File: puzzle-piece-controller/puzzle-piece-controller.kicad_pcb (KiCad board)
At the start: 2 copper layers, 10 parts, among them J1 POGO PINS, J2 OUTPUT_1, J4 BUTTON, J5 Conn_01x04_Socket, U1 MOUDLE-SEEEDUINO-XIAO-ESP32C3

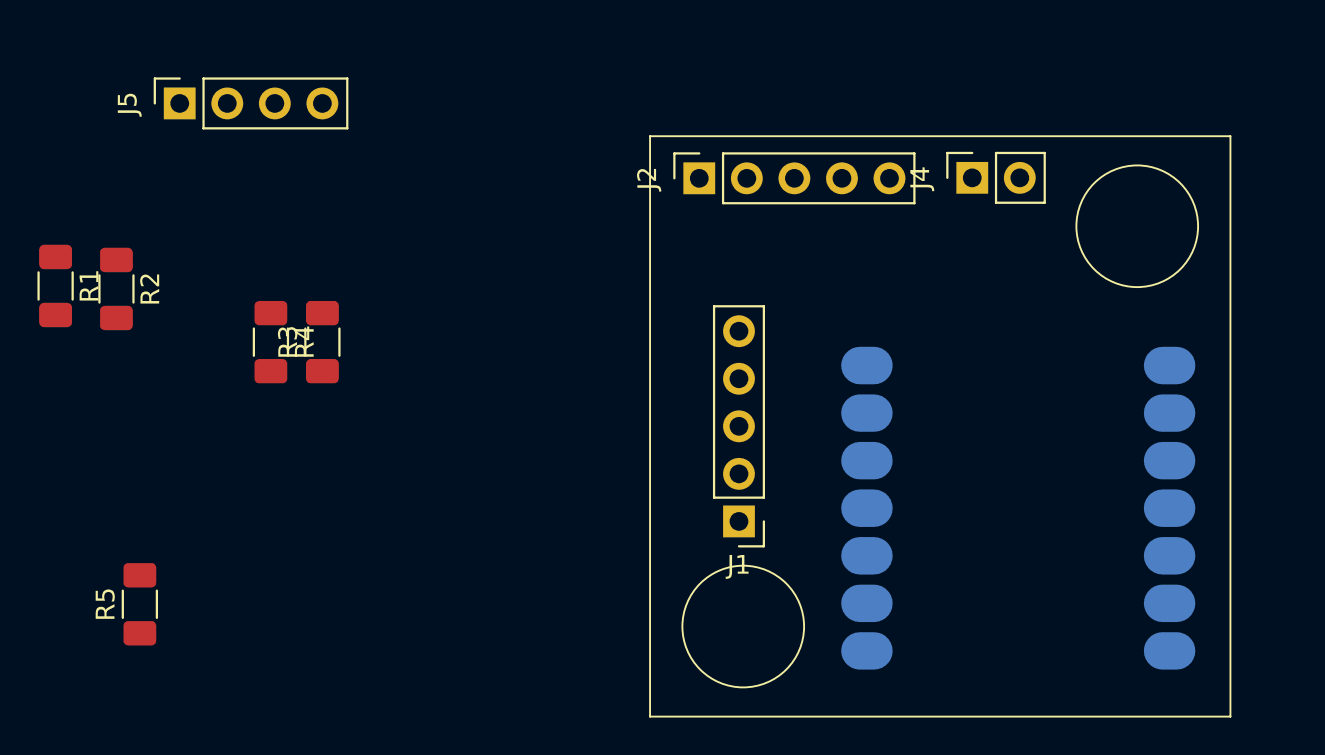
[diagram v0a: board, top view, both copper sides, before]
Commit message: made battery controller singled sided and removed lipo
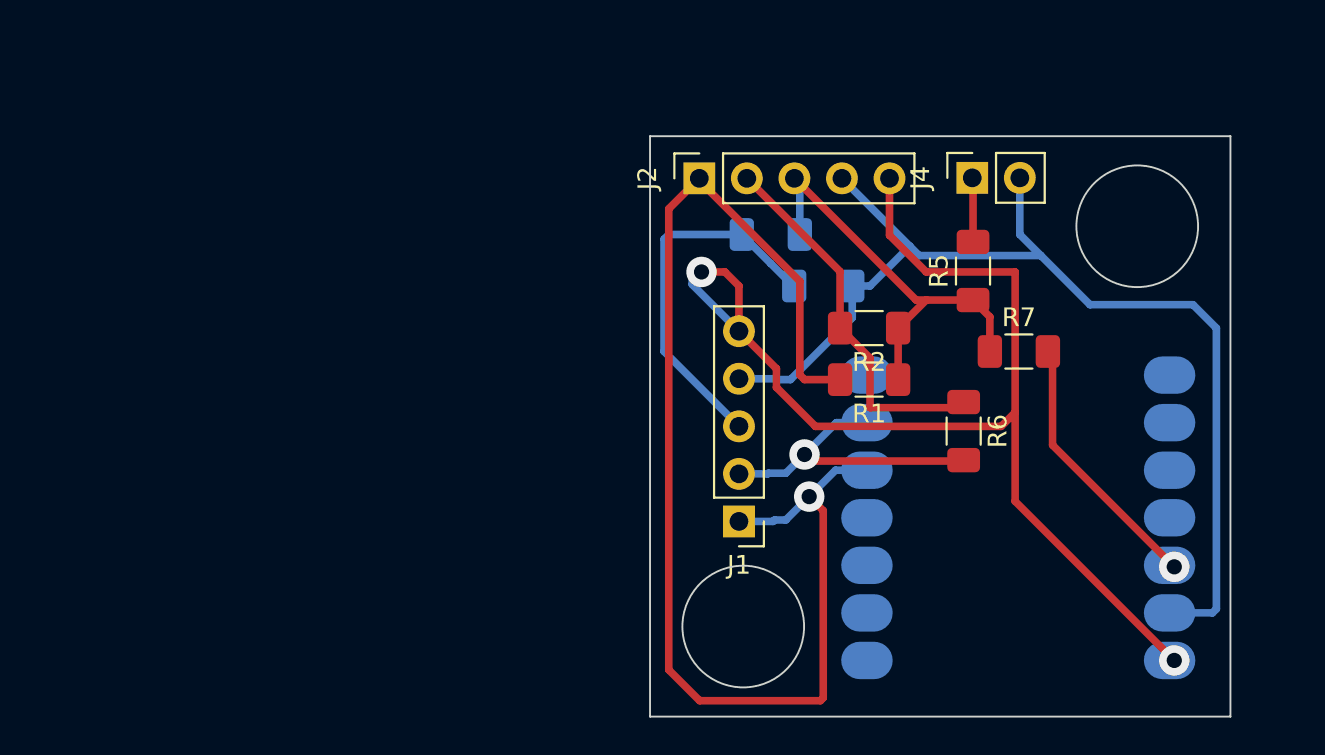
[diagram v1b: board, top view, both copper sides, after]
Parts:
- removed J5: Conn_01x04_Socket, Connector_PinSocket_2.54mm:PinSocket_1x04_P2.54mm_Vertical
- added R6: 0, Resistor_SMD:R_1206_3216Metric_Pad1.30x1.75mm_HandSolder, F.Cu at (224.2, 90.8)
- added R7: 0, Resistor_SMD:R_1206_3216Metric_Pad1.30x1.75mm_HandSolder, F.Cu at (227.2, 86.5)
- R3, R4: moved to B.Cu
- moved R5 47.9 mm to (224.8, 82.2)
- moved R1 43.7 mm to (219.2, 88.0), turned to 180 degrees
- moved R2 40.3 mm to (219.2, 85.2), turned to 180 degrees
- moved R4 29.7 mm to (216.8, 83.0), turned to 0 degrees
- moved R3 24.6 mm to (213.9, 80.2), turned to 180 degrees
- moved U1 0.51 mm to (218.2, 84.9)
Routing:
- net H_SDA: track 0.00 -> 69.9 mm, vias 0 -> 1
- net +5V: track 0.00 -> 62.5 mm, vias 0 -> 2
- net GND: track 0.00 -> 58.6 mm
- net +3.3V: track 0.00 -> 36.8 mm, vias 0 -> 1
- net H_SCL: track 0.00 -> 35.7 mm, vias 0 -> 1
- net ANALOG: track 0.00 -> 19.8 mm
- net Net-(J4-Pin_1): track 0.00 -> 3.44 mm
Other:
- board outline added: 31 x 31 mm

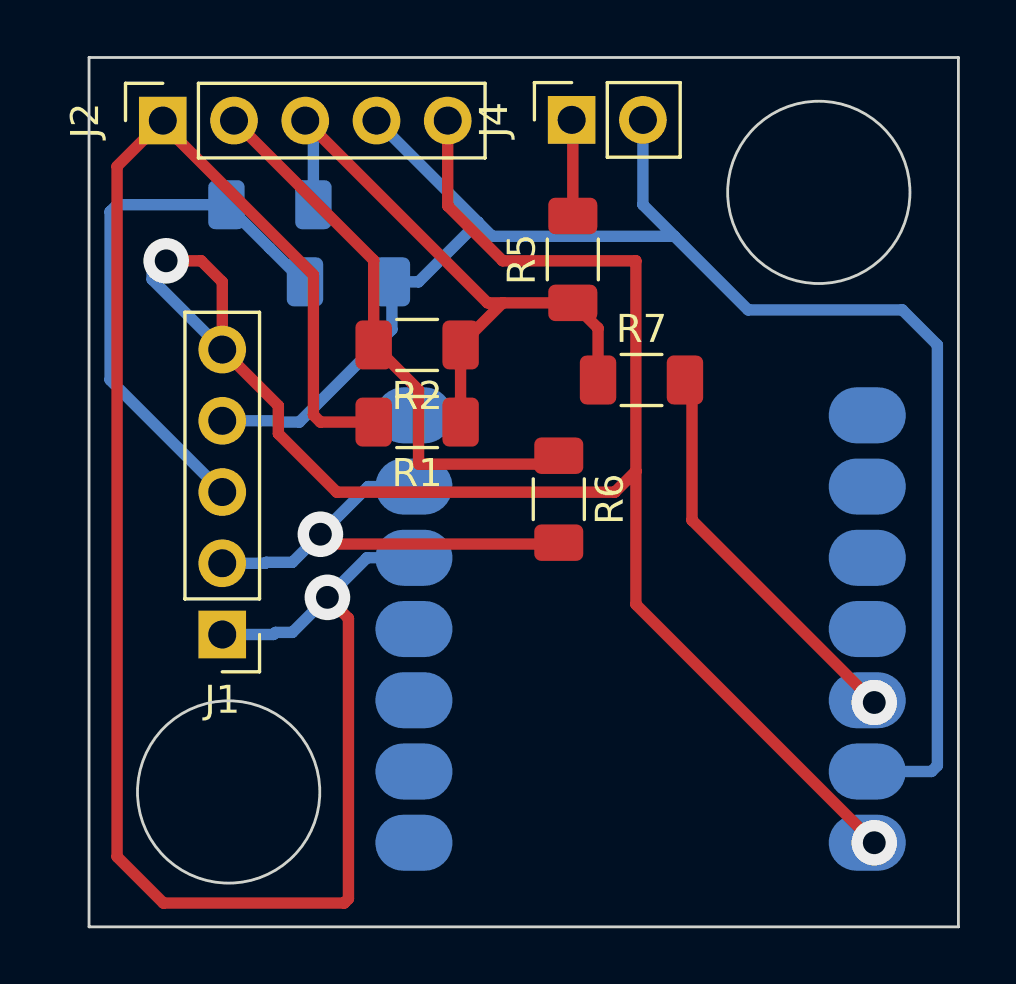
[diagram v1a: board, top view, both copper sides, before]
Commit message: made controller pcb single sided
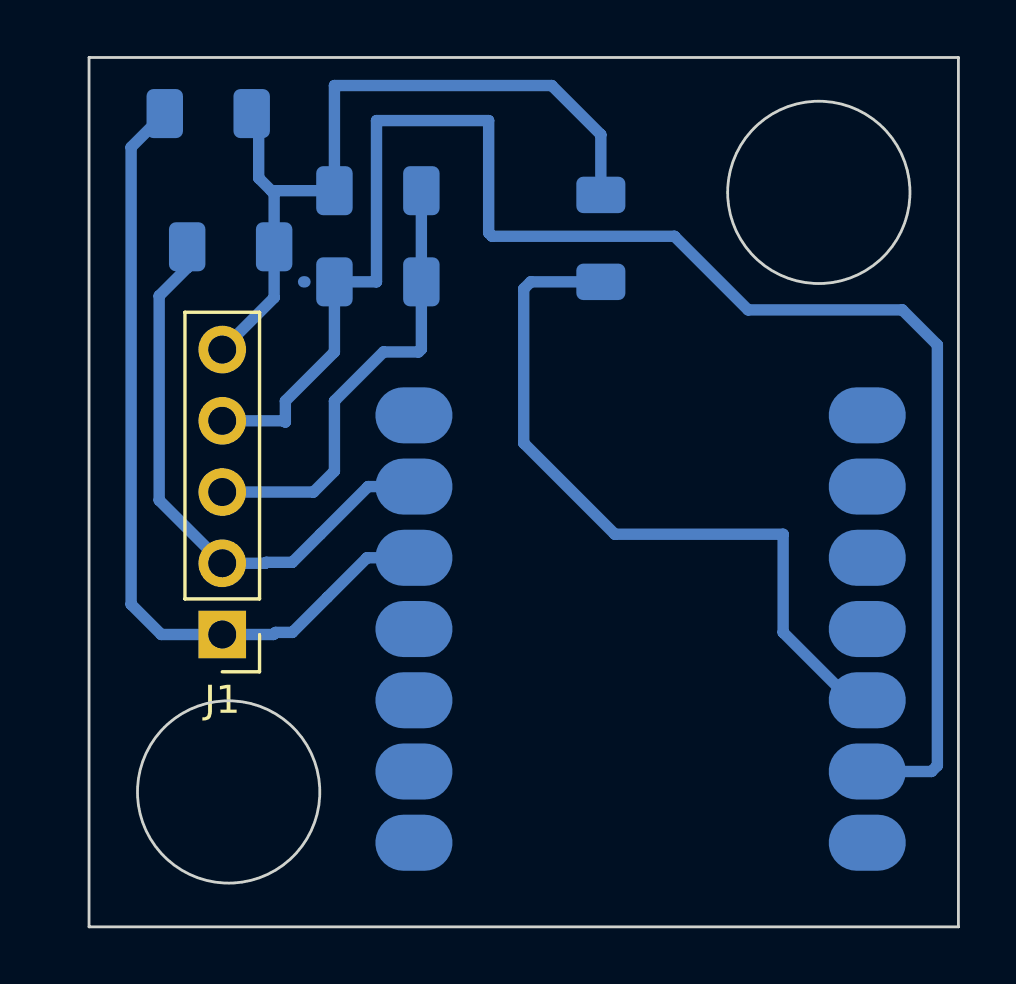
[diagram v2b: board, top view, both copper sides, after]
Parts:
- removed J2: OUTPUT_1, Connector_PinSocket_2.54mm:PinSocket_1x05_P2.54mm_Vertical
- removed J4: BUTTON, Connector_PinSocket_2.54mm:PinSocket_1x02_P2.54mm_Vertical
- removed R5: 10K, Resistor_SMD:R_1206_3216Metric_Pad1.30x1.75mm_HandSolder
- removed R6: 0, Resistor_SMD:R_1206_3216Metric_Pad1.30x1.75mm_HandSolder
- R1, R2, R7: moved to B.Cu
- moved R1 13.3 mm to (211.8, 77.0)
- moved R2 7.51 mm to (212.6, 81.8)
- moved R7 5.25 mm to (225.8, 81.5), turned to -90 degrees
- moved R3 3.88 mm to (217.8, 79.8), turned to 0 degrees
- moved R4 1.05 mm to (217.8, 83.0), turned to 180 degrees
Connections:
- J1 pad 5: +5V -> +3.3V
- U1 pad 1: Net-(J4-Pin_1) -> unconnected-(U1-PA02_A0_D0-Pad1)
- U1 pad 14: +5V -> unconnected-(U1-5V-Pad14)
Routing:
- net +5V: track 62.5 -> 0.00 mm, vias 2 -> 0
- net H_SDA: track 69.9 -> 29.7 mm, vias 1 -> 0
- net +3.3V: track 36.8 -> 54.2 mm, vias 1 -> 0
- net H_SCL: track 35.7 -> 20.6 mm, vias 1 -> 0
- net ANALOG: track 19.8 -> 16.4 mm
- net Net-(J4-Pin_1): track 3.44 -> 0.00 mm

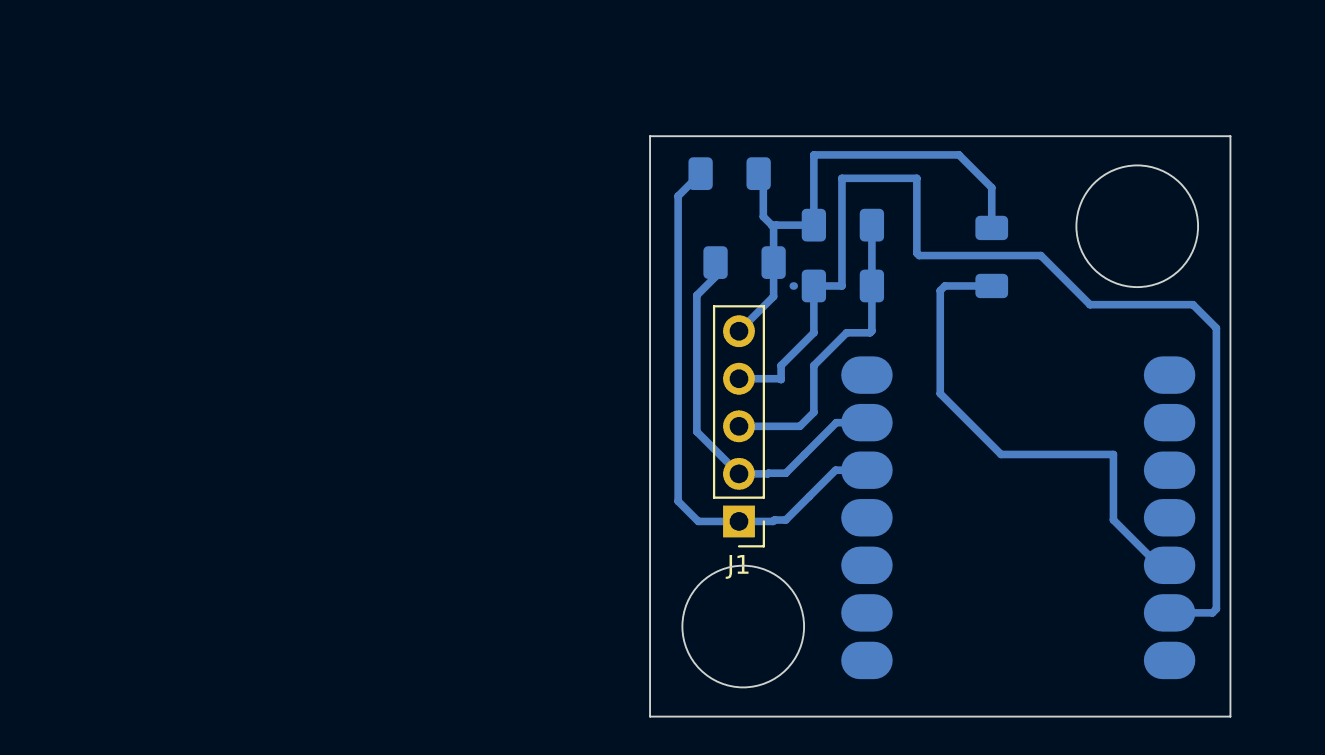
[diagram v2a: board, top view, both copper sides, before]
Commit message: add unrouted output throughholes to controller, and mounting holes
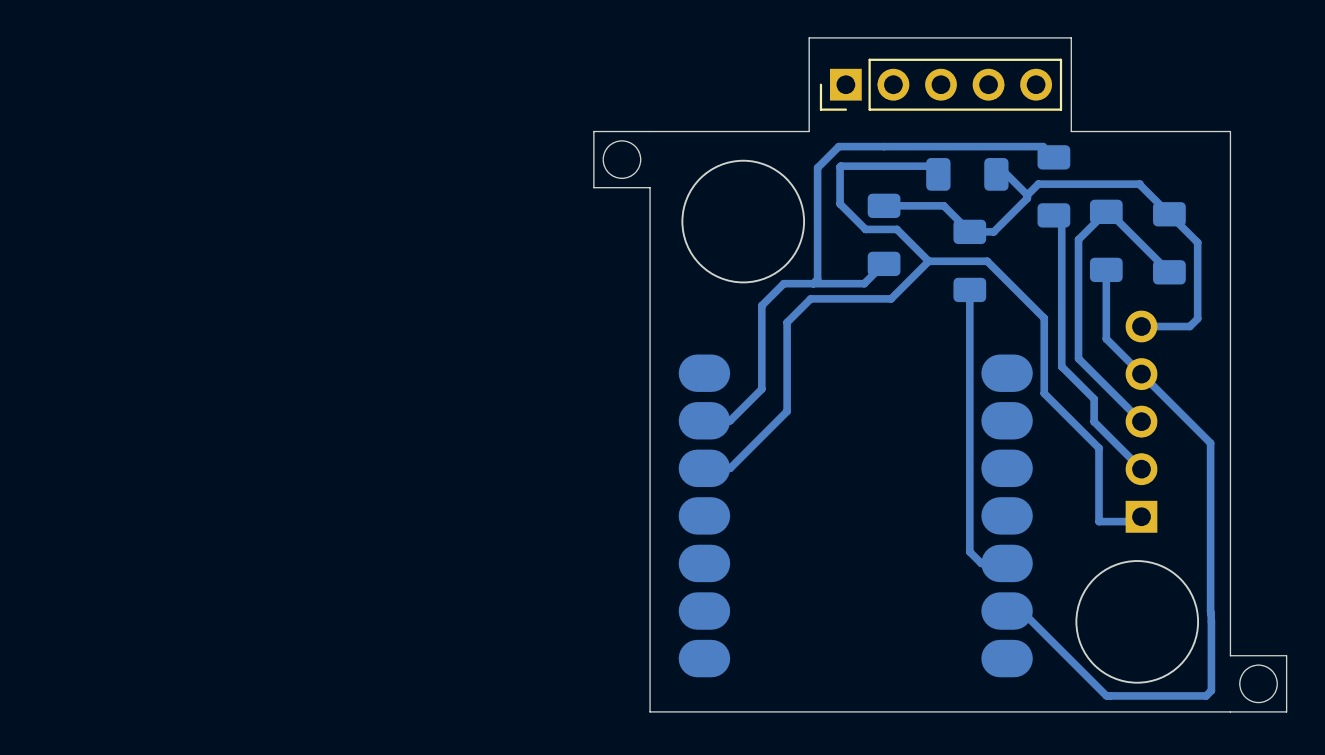
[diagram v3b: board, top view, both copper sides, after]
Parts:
- added J2: OUTPUT, Connector_PinHeader_2.54mm:PinHeader_1x05_P2.54mm_Vertical, F.Cu at (218.0, 72.2)
- added R5: 0, Resistor_SMD:R_1206_3216Metric_Pad1.30x1.75mm_HandSolder, B.Cu at (229.1, 77.7)
- J1: moved to B.Cu
- moved J1 21.5 mm to (233.8, 95.3), turned to 0 degrees
- moved R3 17.5 mm to (235.2, 80.7), turned to -90 degrees
- moved R4 14.3 mm to (231.9, 80.6), turned to -90 degrees
- moved R1 12.7 mm to (224.4, 77.0)
- moved U1 8.68 mm to (209.6, 84.8)
- moved R2 7.60 mm to (220.0, 80.3), turned to -90 degrees
- moved R7 1.19 mm to (224.6, 81.7)
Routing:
- net H_SCL: track 20.6 -> 50.8 mm
- net H_SDA: track 29.7 -> 54.7 mm
- net GND: track 58.5 -> 37.7 mm
- net +3.3V: track 54.2 -> 45.4 mm
- net ANALOG: track 16.4 -> 17.9 mm
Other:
- board size 31 x 31 mm -> 37 x 36 mm

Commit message: made puzzle-controller board double sided
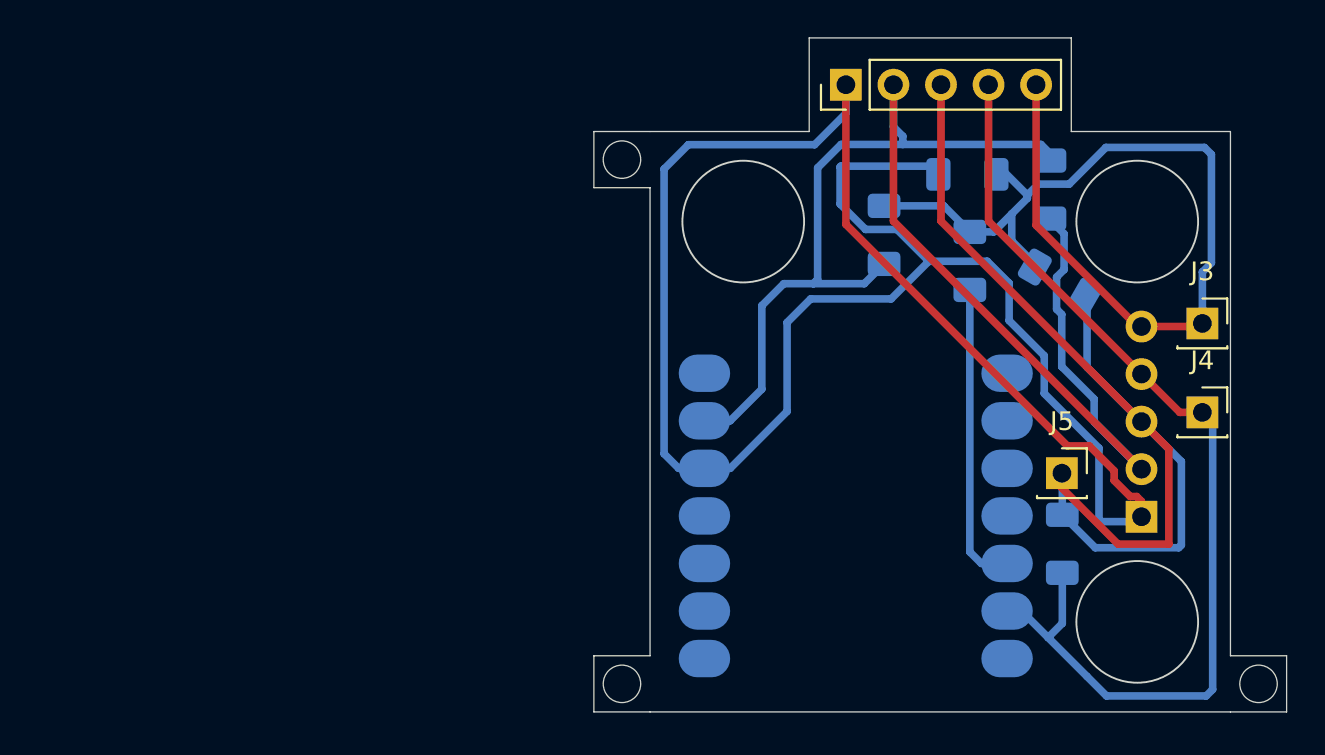
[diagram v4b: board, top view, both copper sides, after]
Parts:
- added J3: 3.3V, Connector_PinSocket_2.54mm:PinSocket_1x01_P2.54mm_Vertical, F.Cu at (237.0, 85.0)
- added J4: GND, Connector_PinSocket_2.54mm:PinSocket_1x01_P2.54mm_Vertical, F.Cu at (237.0, 89.8)
- added J5: ANALOG, Connector_PinSocket_2.54mm:PinSocket_1x01_P2.54mm_Vertical, F.Cu at (229.5, 93.0)
- moved R4 16.3 mm to (229.5, 96.8)
- moved R3 6.19 mm to (229.4, 82.8), turned to -30 degrees
- moved R5 0.27 mm to (228.9, 77.8)
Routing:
- net H_SDA: track 54.7 -> 115.3 mm
- net ANALOG: track 17.9 -> 62.1 mm
- net H_SCL: track 50.8 -> 80.8 mm
- net +3.3V: track 45.4 -> 70.1 mm
- net GND: track 37.7 -> 54.7 mm
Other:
- outline, holes or cut-outs redrawn

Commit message: current puzzle with attiny and pogo pins
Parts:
- removed J5: ANALOG, Connector_PinSocket_2.54mm:PinSocket_1x01_P2.54mm_Vertical
- added J6: OUTPUT, Connector_PinSocket_2.54mm:PinSocket_1x04_P2.54mm_Vertical, F.Cu at (219.1, 71.8)
- J1: moved to F.Cu
- J2: value OUTPUT -> ANALOG; footprint Connector_PinHeader_2.54mm:PinHeader_1x05_P2.54mm_Vertical -> Connector_PinSocket_2.54mm:PinSocket_1x01_P2.54mm_Vertical
- U1: footprint xiao ESP32C3_PCB:MOUDLE14P-SMD-2.54-21X17.8MM -> fab:SeeedStudio_XIAO_ESP32C3
- moved J2 24.4 mm to (229.6, 93.7), turned to 0 degrees
- moved U1 13.5 mm to (218.2, 95.2)
- moved J4 0.85 mm to (237.3, 89.0)
- moved J3 0.52 mm to (237.3, 85.4)
- moved R4 0.17 mm to (229.7, 96.7)
- turned J1 to 180 degrees
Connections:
- J2 pad 1: H_SDA -> ANALOG
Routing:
- net ANALOG: track 62.1 -> 39.9 mm
- net H_SDA: track 115.3 -> 117.0 mm
- net +3.3V: track 70.1 -> 71.1 mm
- net H_SCL: track 80.8 -> 81.8 mm
- net GND: track 54.7 -> 54.2 mm
